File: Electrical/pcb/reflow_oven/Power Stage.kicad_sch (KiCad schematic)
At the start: 13 parts, among them J1 1711738, U1 LH05-10B05, U2 AP1117-33

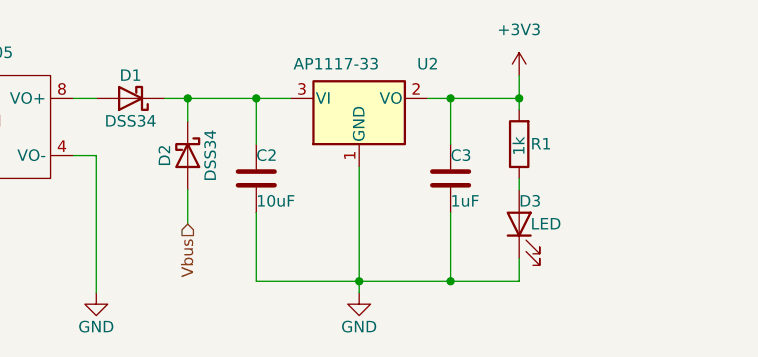
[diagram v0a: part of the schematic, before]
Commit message: schematic
added microcontrroller and .ioc file
added usb serial converter
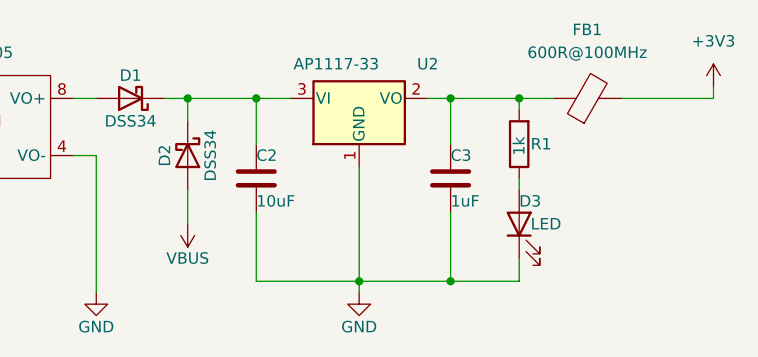
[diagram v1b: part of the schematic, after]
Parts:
- added FB1: 600R@100MHz, Resistor_SMD:R_0603_1608Metric_Pad0.98x0.95mm_HandSolder, symbol Device:FerriteBead
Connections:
- net +3V3: now also FB1.2; no longer C3.1, R1.2, U2.2 (VO)
- net Vbus renamed VBUS
- new net: C3.1, FB1.1, R1.2, U2.2 (VO)
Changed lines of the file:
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@@
   (junction (at 119.38 88.9) (diameter 0) (color 0 0 0 0)
   )
+  (junction (at 196.85 109.22) (diameter 0) (color 0 0 0 0)
+  )
+  (junction (at 119.38 99.06) (diameter 0) (color 0 0 0 0)
+  )
   (junction (at 214.63 88.9) (diameter 0) (color 0 0 0 0)
   )
-  (junction (at 196.85 109.22) (diameter 0) (color 0 0 0 0)
-  )
-  (junction (at 119.38 99.06) (diameter 0) (color 0 0 0 0)
-  )
   (junction (at 207.01 88.9) (diameter 0) (color 0 0 0 0)
   )
@@
     (stroke (width 0) (type default) (color 0 0 0 0))
   )
-  (wire (pts (xy 214.63 86.36) (xy 214.63 88.9))
+  (wire (pts (xy 226.06 88.9) (xy 236.22 88.9))
     (stroke (width 0) (type default) (color 0 0 0 0))
   )
@@
     (stroke (width 0) (type default) (color 0 0 0 0))
   )
+  (wire (pts (xy 214.63 88.9) (xy 218.44 88.9))
+    (stroke (width 0) (type default) (color 0 0 0 0))
+  )
   (wire (pts (xy 185.42 88.9) (xy 185.42 93.98))
     (stroke (width 0) (type default) (color 0 0 0 0))
@@
   )
   (wire (pts (xy 88.9 88.9) (xy 90.17 88.9))
+    (stroke (width 0) (type default) (color 0 0 0 0))
+  )
+  (wire (pts (xy 236.22 88.9) (xy 236.22 87.63))
     (stroke (width 0) (type default) (color 0 0 0 0))
   )
@@
     (effects (font (size 1.27 1.27)) (justify left bottom))
   )
-  (hierarchical_label "Vbus" (shape input) (at 177.8 102.87 270)
-    (effects (font (size 1.27 1.27)) (justify right))
-  )
   (symbol (lib_id "Device:C") (at 127 93.98 0) (unit 1)
     (in_bom yes) (on_board yes)
@@
   (symbol (lib_id "power:GND") (at 196.85 110.49 0) (unit 1)
     (in_bom yes) (on_board yes)
-    (property "Reference" "#PWR04" (id 0) (at 196.85 116.84 0)
+    (property "Reference" "#PWR05" (id 0) (at 196.85 116.84 0)
       (effects (font (size 1.27 1.27)) hide)
     )
@@
     (pin "2")
   )
+  (symbol (lib_id "power:VBUS") (at 177.8 102.87 180) (unit 1)
+    (in_bom yes) (on_board yes)
+    (property "Reference" "#PWR04" (id 0) (at 177.8 99.06 0)
+      (effects (font (size 1.27 1.27)) hide)
+    )
+    (property "Value" "VBUS" (id 1) (at 177.8 106.68 0))
+    (property "Footprint" "" (id 2) (at 177.8 102.87 0)
+      (effects (font (size 1.27 1.27)) hide)
+    )
+    (property "Datasheet" "" (id 3) (at 177.8 102.87 0)
+      (effects (font (size 1.27 1.27)) hide)
+    )
+    (pin "1")
+  )
   (symbol (lib_id "power:GNDREF") (at 138.43 102.87 0) (unit 1)
     (in_bom yes) (on_board yes) (fields_autoplaced)
@@
     (pin "1")
   )
-  (symbol (lib_id "power:+3V3") (at 214.63 86.36 0) (unit 1)
+  (symbol (lib_id "power:+3V3") (at 236.22 87.63 0) (unit 1)
     (in_bom yes) (on_board yes) (fields_autoplaced)
-    (property "Reference" "#PWR05" (id 0) (at 214.63 90.17 0)
-      (effects (font (size 1.27 1.27)) hide)
-    )
-    (property "Value" "+3V3" (id 1) (at 214.63 81.28 0))
-    (property "Footprint" "" (id 2) (at 214.63 86.36 0)
-      (effects (font (size 1.27 1.27)) hide)
-    )
-    (property "Datasheet" "" (id 3) (at 214.63 86.36 0)
+    (property "Reference" "#PWR06" (id 0) (at 236.22 91.44 0)
+      (effects (font (size 1.27 1.27)) hide)
+    )
+    (property "Value" "+3V3" (id 1) (at 236.22 82.55 0))
+    (property "Footprint" "" (id 2) (at 236.22 87.63 0)
+      (effects (font (size 1.27 1.27)) hide)
+    )
+    (property "Datasheet" "" (id 3) (at 236.22 87.63 0)
       (effects (font (size 1.27 1.27)) hide)
     )
@@
     (pin "8")
   )
+  (symbol (lib_id "Device:FerriteBead") (at 222.25 88.9 90) (unit 1)
+    (in_bom yes) (on_board yes) (fields_autoplaced)
+    (property "Reference" "FB1" (id 0) (at 222.1992 81.28 90))
+    (property "Value" "600R@100MHz" (id 1) (at 222.1992 83.82 90))
+    (property "Footprint" "Resistor_SMD:R_0603_1608Metric_Pad0.98x0.95mm_HandSolder" (id 2) (at 222.25 90.678 90)
+      (effects (font (size 1.27 1.27)) hide)
+    )
+    (property "Datasheet" "~" (id 3) (at 222.25 88.9 0)
+      (effects (font (size 1.27 1.27)) hide)
+    )
+    (pin "1")
+    (pin "2")
+  )
   (symbol (lib_id "power:GND") (at 167.64 110.49 0) (unit 1)

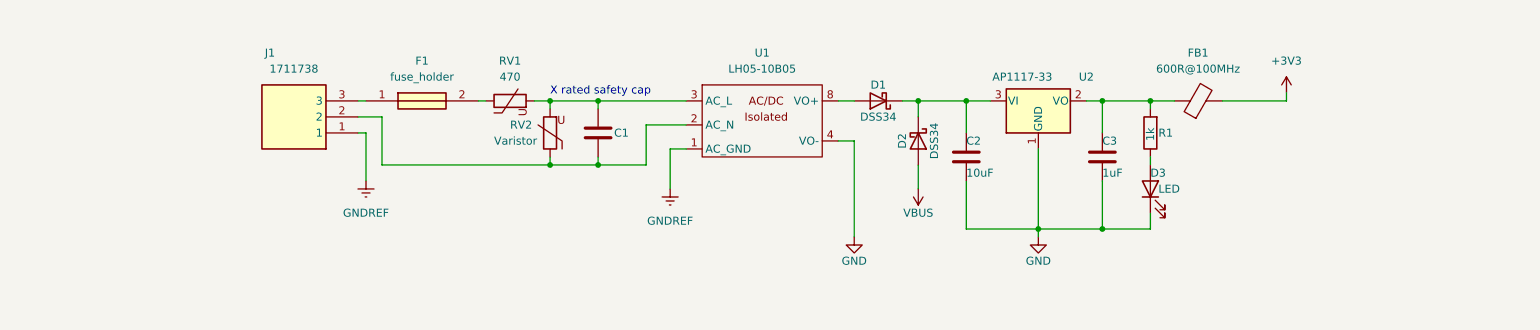
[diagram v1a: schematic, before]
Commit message: interface
partial interface schematic
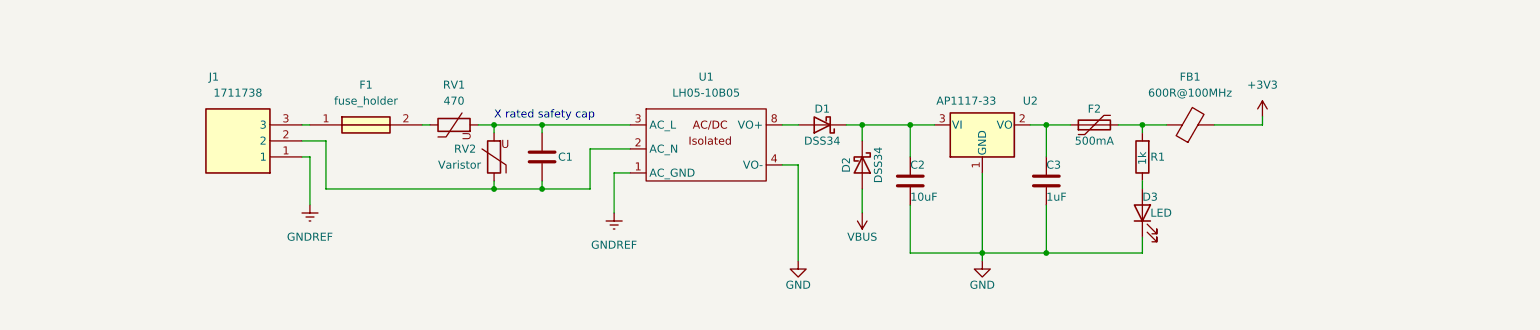
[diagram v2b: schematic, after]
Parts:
- added F2: 500mA, Fuse:Fuse_1206_3216Metric_Pad1.42x1.75mm_HandSolder, symbol Device:Polyfuse
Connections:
- net at C3.1, U2.2 (VO): now also F2.1; no longer FB1.1, R1.2
- new net: F2.2, FB1.1, R1.2
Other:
- moved on the sheet: C1, C2, C3, D1, D2, F1, J1, RV1, RV2, U1, U2

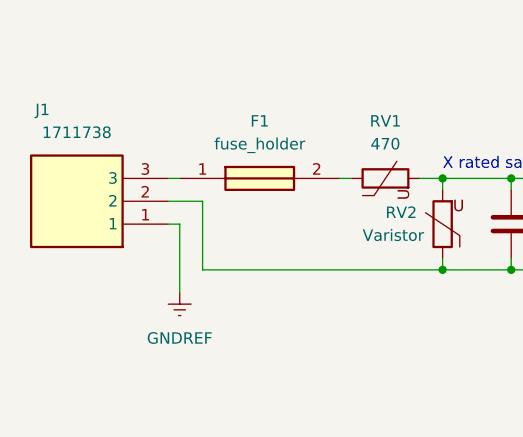
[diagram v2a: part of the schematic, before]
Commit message: analog Sensing
-voltage and current sensor
-zero crossing
-temperature
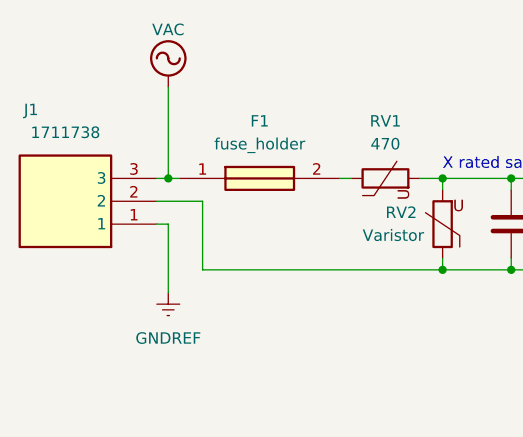
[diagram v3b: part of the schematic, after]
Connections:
- net VAC: now reaches F1.1, J1.3
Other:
- moved on the sheet: J1
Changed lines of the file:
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@@
   (junction (at 198.12 92.71) (diameter 0) (color 0 0 0 0)
   )
+  (junction (at 80.01 92.71) (diameter 0) (color 0 0 0 0)
+  )
   (junction (at 198.12 113.03) (diameter 0) (color 0 0 0 0)
   )
@@
     (stroke (width 0) (type default) (color 0 0 0 0))
   )
+  (wire (pts (xy 83.82 102.87) (xy 110.49 102.87))
+    (stroke (width 0) (type default) (color 0 0 0 0))
+  )
   (wire (pts (xy 132.08 100.33) (xy 129.54 100.33))
     (stroke (width 0) (type default) (color 0 0 0 0))
@@
     (stroke (width 0) (type default) (color 0 0 0 0))
   )
+  (wire (pts (xy 80.01 82.55) (xy 80.01 92.71))
+    (stroke (width 0) (type default) (color 0 0 0 0))
+  )
   (wire (pts (xy 125.73 96.52) (xy 125.73 102.87))
     (stroke (width 0) (type default) (color 0 0 0 0))
@@
     (stroke (width 0) (type default) (color 0 0 0 0))
   )
+  (wire (pts (xy 118.11 102.87) (xy 125.73 102.87))
+    (stroke (width 0) (type default) (color 0 0 0 0))
+  )
   (wire (pts (xy 187.96 100.33) (xy 187.96 113.03))
     (stroke (width 0) (type default) (color 0 0 0 0))
@@
     (stroke (width 0) (type default) (color 0 0 0 0))
   )
-  (wire (pts (xy 81.28 97.79) (xy 81.28 105.41))
+  (wire (pts (xy 80.01 97.79) (xy 80.01 105.41))
     (stroke (width 0) (type default) (color 0 0 0 0))
   )
@@
     (stroke (width 0) (type default) (color 0 0 0 0))
   )
-  (wire (pts (xy 83.82 102.87) (xy 110.49 102.87))
-    (stroke (width 0) (type default) (color 0 0 0 0))
-  )
   (wire (pts (xy 156.21 99.06) (xy 158.75 99.06))
     (stroke (width 0) (type default) (color 0 0 0 0))
@@
     (stroke (width 0) (type default) (color 0 0 0 0))
   )
-  (wire (pts (xy 118.11 102.87) (xy 125.73 102.87))
-    (stroke (width 0) (type default) (color 0 0 0 0))
-  )
   (wire (pts (xy 132.08 96.52) (xy 125.73 96.52))
     (stroke (width 0) (type default) (color 0 0 0 0))
@@
     (stroke (width 0) (type default) (color 0 0 0 0))
   )
-  (wire (pts (xy 80.01 95.25) (xy 83.82 95.25))
-    (stroke (width 0) (type default) (color 0 0 0 0))
-  )
-  (wire (pts (xy 80.01 97.79) (xy 81.28 97.79))
+  (wire (pts (xy 78.74 95.25) (xy 83.82 95.25))
+    (stroke (width 0) (type default) (color 0 0 0 0))
+  )
+  (wire (pts (xy 78.74 97.79) (xy 80.01 97.79))
     (stroke (width 0) (type default) (color 0 0 0 0))
   )
@@
     (stroke (width 0) (type default) (color 0 0 0 0))
   )
+  (wire (pts (xy 80.01 92.71) (xy 81.28 92.71))
+    (stroke (width 0) (type default) (color 0 0 0 0))
+  )
   (wire (pts (xy 198.12 97.79) (xy 198.12 92.71))
     (stroke (width 0) (type default) (color 0 0 0 0))
   )
-  (wire (pts (xy 80.01 92.71) (xy 81.28 92.71))
+  (wire (pts (xy 78.74 92.71) (xy 80.01 92.71))
     (stroke (width 0) (type default) (color 0 0 0 0))
   )
@@
   (symbol (lib_id "power:GND") (at 187.96 114.3 0) (unit 1)
     (in_bom yes) (on_board yes)
-    (property "Reference" "#PWR05" (id 0) (at 187.96 120.65 0)
+    (property "Reference" "#PWR06" (id 0) (at 187.96 120.65 0)
       (effects (font (size 1.27 1.27)) hide)
     )
@@
     (pin "2")
   )
-  (symbol (lib_id "comp_lib:1711738") (at 80.01 97.79 180) (unit 1)
-    (in_bom yes) (on_board yes)
-    (property "Reference" "J1" (id 0) (at 66.04 85.09 0))
-    (property "Value" "1711738" (id 1) (at 69.85 87.63 0))
-    (property "Footprint" "footprint_lib:1711738" (id 2) (at 80.01 97.79 0)
-      (effects (font (size 1.27 1.27)) hide)
-    )
-    (property "Datasheet" ".\\datasheets\\phoenix-contact-1711738-en.pdf" (id 3) (at 80.01 97.79 0)
-      (effects (font (size 1.27 1.27)) hide)
-    )
-    (property "Reference_1" "J" (id 4) (at 63.5 105.41 0)
-      (effects (font (size 1.27 1.27)) (justify left top) hide)
-    )
-    (property "Value_1" "1711738" (id 5) (at 63.5 102.87 0)
-      (effects (font (size 1.27 1.27)) (justify left top) hide)
-    )
-    (property "Footprint_1" "1711738" (id 6) (at 63.5 2.87 0)
-      (effects (font (size 1.27 1.27)) (justify left top) hide)
-    )
-    (property "Datasheet_1" "http://www.phoenixcontact.com/de/produkte/1711738/pdf" (id 7) (at 63.5 -97.13 0)
-      (effects (font (size 1.27 1.27)) (justify left top) hide)
-    )
-    (property "Height" "18.2" (id 8) (at 63.5 -297.13 0)
-      (effects (font (size 1.27 1.27)) (justify left top) hide)
-    )
-    (property "Mouser Part Number" "651-1711738" (id 9) (at 63.5 -397.13 0)
-      (effects (font (size 1.27 1.27)) (justify left top) hide)
-    )
-    (property "Mouser Price/Stock" "https://www.mouser.co.uk/ProductDetail/Phoenix-Contact/1711738?qs=F79NelsxgYGJoCQSSUE92w%3D%3D" (id 10) (at 63.5 -497.13 0)
-      (effects (font (size 1.27 1.27)) (justify left top) hide)
-    )
-    (property "Manufacturer_Name" "Phoenix Contact" (id 11) (at 63.5 -597.13 0)
-      (effects (font (size 1.27 1.27)) (justify left top) hide)
-    )
-    (property "Manufacturer_Part_Number" "1711738" (id 12) (at 63.5 -697.13 0)
+  (symbol (lib_id "comp_lib:1711738") (at 78.74 97.79 180) (unit 1)
+    (in_bom yes) (on_board yes)
+    (property "Reference" "J1" (id 0) (at 64.77 85.09 0))
+    (property "Value" "1711738" (id 1) (at 68.58 87.63 0))
+    (property "Footprint" "footprint_lib:1711738" (id 2) (at 78.74 97.79 0)
+      (effects (font (size 1.27 1.27)) hide)
+    )
+    (property "Datasheet" ".\\datasheets\\phoenix-contact-1711738-en.pdf" (id 3) (at 78.74 97.79 0)
+      (effects (font (size 1.27 1.27)) hide)
+    )
+    (property "Reference_1" "J" (id 4) (at 62.23 105.41 0)
+      (effects (font (size 1.27 1.27)) (justify left top) hide)
+    )
+    (property "Value_1" "1711738" (id 5) (at 62.23 102.87 0)
+      (effects (font (size 1.27 1.27)) (justify left top) hide)
+    )
+    (property "Footprint_1" "1711738" (id 6) (at 62.23 2.87 0)
+      (effects (font (size 1.27 1.27)) (justify left top) hide)
+    )
+    (property "Datasheet_1" "http://www.phoenixcontact.com/de/produkte/1711738/pdf" (id 7) (at 62.23 -97.13 0)
+      (effects (font (size 1.27 1.27)) (justify left top) hide)
+    )
+    (property "Height" "18.2" (id 8) (at 62.23 -297.13 0)
+      (effects (font (size 1.27 1.27)) (justify left top) hide)
+    )
+    (property "Mouser Part Number" "651-1711738" (id 9) (at 62.23 -397.13 0)
+      (effects (font (size 1.27 1.27)) (justify left top) hide)
+    )
+    (property "Mouser Price/Stock" "https://www.mouser.co.uk/ProductDetail/Phoenix-Contact/1711738?qs=F79NelsxgYGJoCQSSUE92w%3D%3D" (id 10) (at 62.23 -497.13 0)
+      (effects (font (size 1.27 1.27)) (justify left top) hide)
+    )
+    (property "Manufacturer_Name" "Phoenix Contact" (id 11) (at 62.23 -597.13 0)
+      (effects (font (size 1.27 1.27)) (justify left top) hide)
+    )
+    (property "Manufacturer_Part_Number" "1711738" (id 12) (at 62.23 -697.13 0)
       (effects (font (size 1.27 1.27)) (justify left top) hide)
     )
@@
   (symbol (lib_id "power:VBUS") (at 168.91 106.68 180) (unit 1)
     (in_bom yes) (on_board yes)
-    (property "Reference" "#PWR04" (id 0) (at 168.91 102.87 0)
+    (property "Reference" "#PWR05" (id 0) (at 168.91 102.87 0)
       (effects (font (size 1.27 1.27)) hide)
     )
@@
   (symbol (lib_id "power:GNDREF") (at 129.54 106.68 0) (unit 1)
     (in_bom yes) (on_board yes) (fields_autoplaced)
-    (property "Reference" "#PWR02" (id 0) (at 129.54 113.03 0)
+    (property "Reference" "#PWR03" (id 0) (at 129.54 113.03 0)
       (effects (font (size 1.27 1.27)) hide)
     )
@@
     (pin "1")
   )
-  (symbol (lib_id "power:GNDREF") (at 81.28 105.41 0) (unit 1)
+  (symbol (lib_id "power:GNDREF") (at 80.01 105.41 0) (unit 1)
     (in_bom yes) (on_board yes) (fields_autoplaced)
-    (property "Reference" "#PWR01" (id 0) (at 81.28 111.76 0)
-      (effects (font (size 1.27 1.27)) hide)
-    )
-    (property "Value" "GNDREF" (id 1) (at 81.28 110.49 0))
-    (property "Footprint" "" (id 2) (at 81.28 105.41 0)
-      (effects (font (size 1.27 1.27)) hide)
-    )
-    (property "Datasheet" "" (id 3) (at 81.28 105.41 0)
+    (property "Reference" "#PWR02" (id 0) (at 80.01 111.76 0)
+      (effects (font (size 1.27 1.27)) hide)
+    )
+    (property "Value" "GNDREF" (id 1) (at 80.01 110.49 0))
+    (property "Footprint" "" (id 2) (at 80.01 105.41 0)
+      (effects (font (size 1.27 1.27)) hide)
+    )
+    (property "Datasheet" "" (id 3) (at 80.01 105.41 0)
       (effects (font (size 1.27 1.27)) hide)
     )
@@
   (symbol (lib_id "power:+3V3") (at 232.41 91.44 0) (unit 1)
     (in_bom yes) (on_board yes) (fields_autoplaced)
-    (property "Reference" "#PWR06" (id 0) (at 232.41 95.25 0)
+    (property "Reference" "#PWR07" (id 0) (at 232.41 95.25 0)
       (effects (font (size 1.27 1.27)) hide)
     )
@@
     (pin "8")
   )
+  (symbol (lib_id "power:VAC") (at 80.01 82.55 0) (unit 1)
+    (in_bom yes) (on_board yes)
+    (property "Reference" "#PWR01" (id 0) (at 80.01 85.09 0)
+      (effects (font (size 1.27 1.27)) hide)
+    )
+    (property "Value" "VAC" (id 1) (at 80.01 76.2 0))
+    (property "Footprint" "" (id 2) (at 80.01 82.55 0)
+      (effects (font (size 1.27 1.27)) hide)
+    )
+    (property "Datasheet" "" (id 3) (at 80.01 82.55 0)
+      (effects (font (size 1.27 1.27)) hide)
+    )
+    (pin "1")
+  )
   (symbol (lib_id "power:GND") (at 158.75 114.3 0) (unit 1)
     (in_bom yes) (on_board yes)
-    (property "Reference" "#PWR03" (id 0) (at 158.75 120.65 0)
-      (effects (font (size 1.27 1.27)) hide)
-    )
+    (property "Reference" "#PWR04" (id 0) (at 158.75 120.65 0)
+      (effects (font (size 1.27 1.27)) hide)
+    )

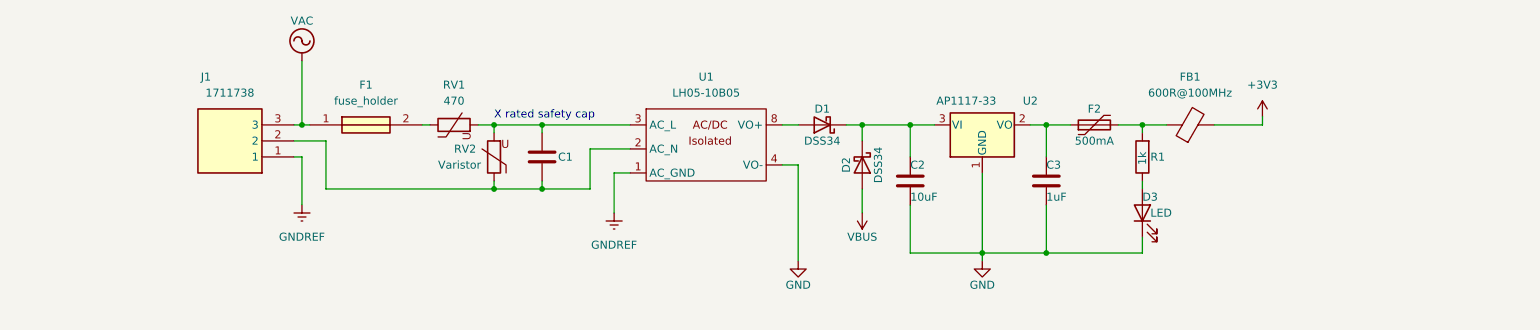
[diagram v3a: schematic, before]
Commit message: functionality
done output stage
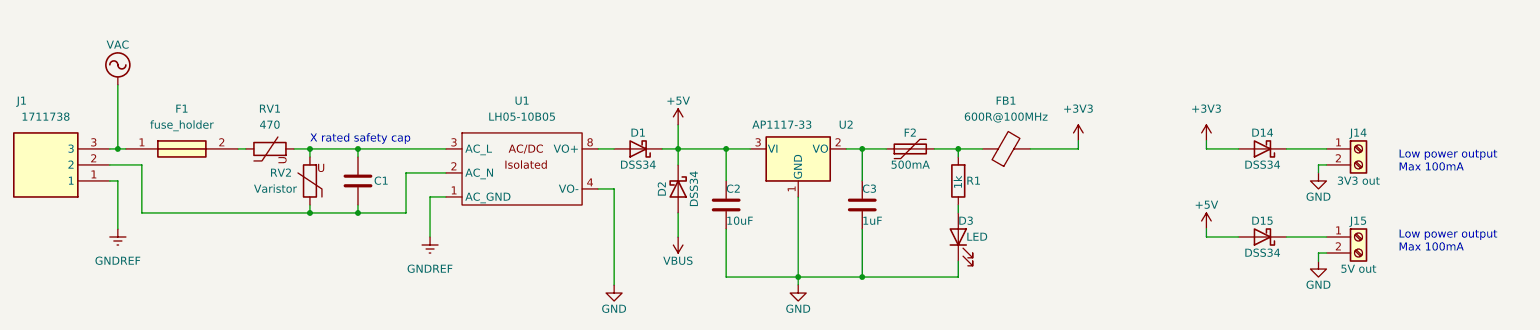
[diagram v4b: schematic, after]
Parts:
- added D14, D15: DSS34, Diode_SMD:D_SOD-123F, symbol Device:D_Schottky
- added J14: 3V3 out, TerminalBlock_Phoenix:TerminalBlock_Phoenix_MPT-0,5-2-2.54_1x02_P2.54mm_Horizontal, symbol Connector:Screw_Terminal_01x02
- added J15: 5V out, TerminalBlock_Phoenix:TerminalBlock_Phoenix_MPT-0,5-2-2.54_1x02_P2.54mm_Horizontal, symbol Connector:Screw_Terminal_01x02
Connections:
- net +3V3: now also D14.2 (A)
- net GND: now also J14.2 (Pin_2), J15.2 (Pin_2)
- net +5V: now reaches C2.1, D1.1 (K), D2.1 (K), U2.3 (VI)
- net +5V: now also D15.2 (A)
- new net: D14.1 (K), J14.1 (Pin_1)
- new net: D15.1 (K), J15.1 (Pin_1)
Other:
- note added: "Low power output Max 100mA"
- moved on the sheet: C1, C2, C3, D1, D2, D3, F1, F2, FB1, J1, R1, RV1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
